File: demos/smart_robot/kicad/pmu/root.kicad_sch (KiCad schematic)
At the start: 14 parts, among them U3V3 TPS62162DSG, U5V TPS54331

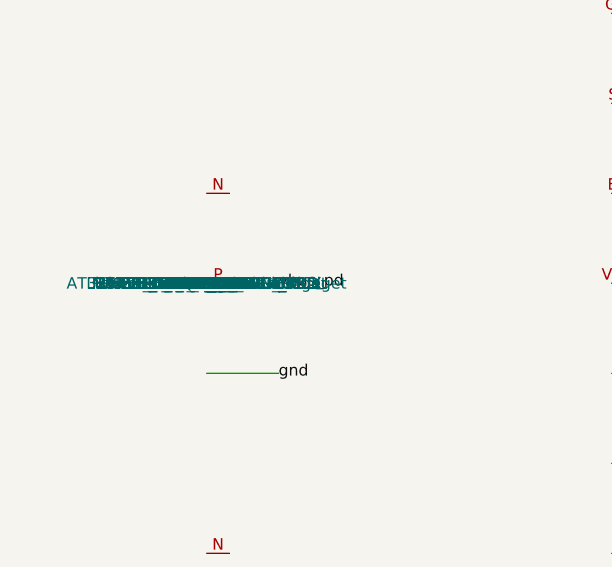
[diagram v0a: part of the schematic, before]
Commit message: Select smart robot servo eFuse
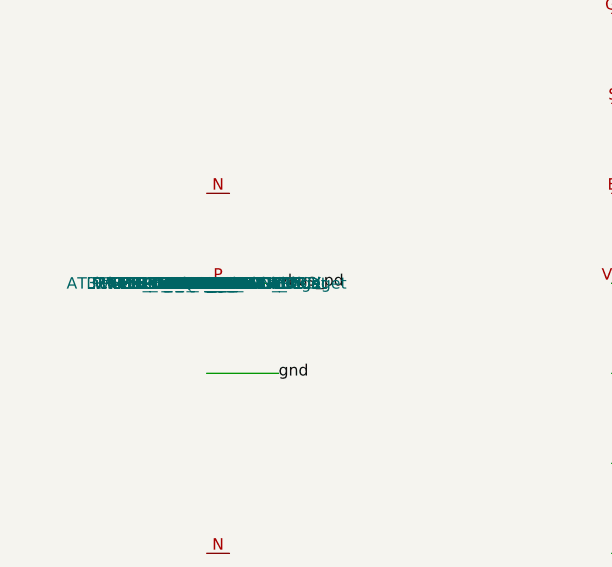
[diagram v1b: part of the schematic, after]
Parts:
- U_SERVO_SW: value SERVO_ESTOP_SWITCH_TBD -> TPS25948-8A-RCB-DVDT
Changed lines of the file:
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@@
   (symbol (lib_id "CircuitCI:EStop_Power_Switch") (at 180 0 0)
     (property "Reference" "U_SERVO_SW")
-    (property "Value" "SERVO_ESTOP_SWITCH_TBD")
+    (property "Value" "TPS25948-8A-RCB-DVDT")
     (pin "VIN") (pin "VOUT") (pin "EN") (pin "GND"))
   (symbol (lib_id "CircuitCI:EStop_Power_Switch") (at 180 60 0)

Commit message: Select smart robot wheel eFuse path
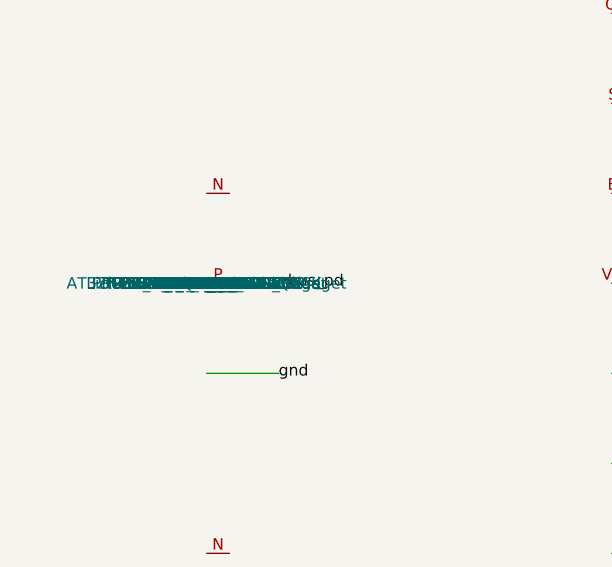
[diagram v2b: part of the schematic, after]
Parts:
- U_WHEEL_SW: value WHEEL_ESTOP_SWITCH_TBD -> TPS24751+CSD17501Q5A
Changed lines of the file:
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@@
   (symbol (lib_id "CircuitCI:EStop_Power_Switch") (at 180 60 0)
     (property "Reference" "U_WHEEL_SW")
-    (property "Value" "WHEEL_ESTOP_SWITCH_TBD")
+    (property "Value" "TPS24751+CSD17501Q5A")
     (pin "VIN") (pin "VOUT") (pin "EN") (pin "GND"))
   (symbol (lib_id "CircuitCI:LicheeRV_Nano_W_Load") (at 225 0 0)
